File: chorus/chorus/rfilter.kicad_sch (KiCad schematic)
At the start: 12 parts

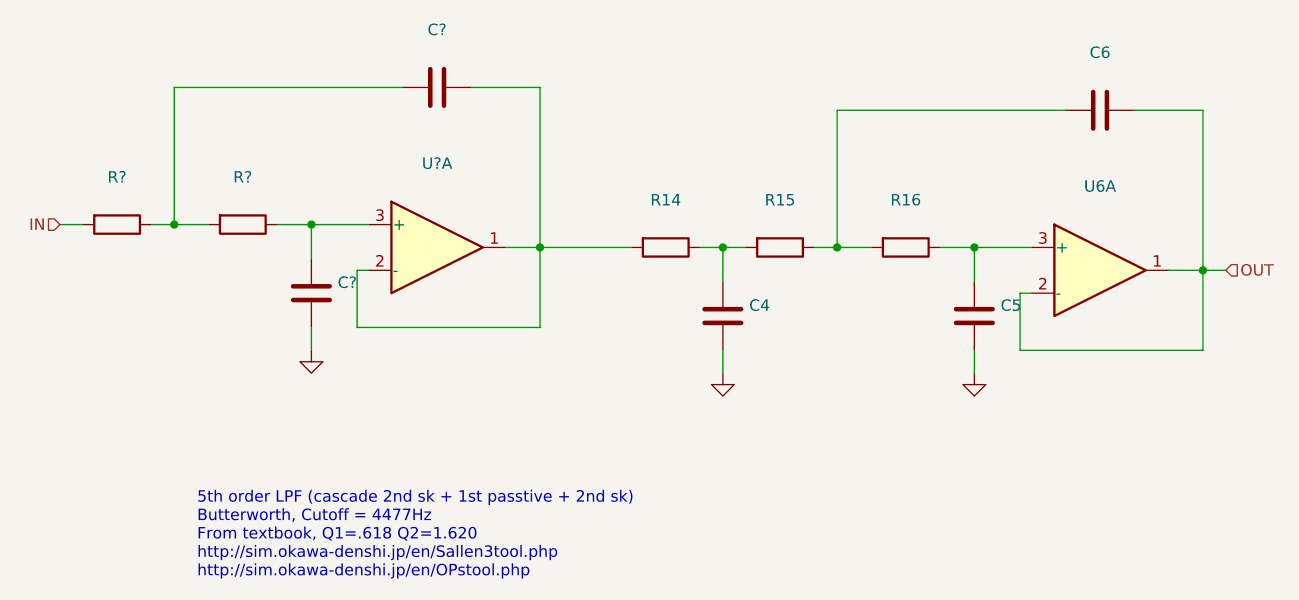
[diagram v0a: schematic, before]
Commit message: add output buffer
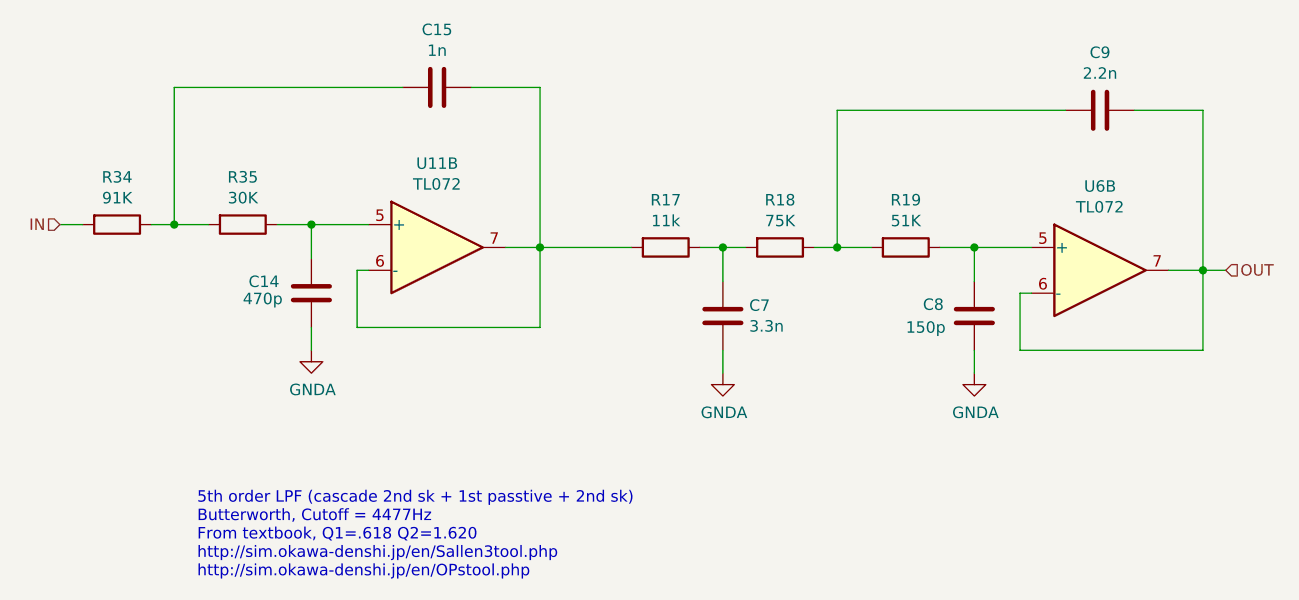
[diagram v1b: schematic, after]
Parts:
- C14: renamed from C?; value (none) -> 470p
- C15: renamed from C?; value (none) -> 1n
- C7: renamed from C4; value (none) -> 3.3n
- C8: renamed from C5; value (none) -> 150p
- C9: renamed from C6; value (none) -> 2.2n
- R17: renamed from R14; value (none) -> 11k
- R18: renamed from R15; value (none) -> 75K
- R19: renamed from R16; value (none) -> 51K
- R34: renamed from R?; value (none) -> 91K
- R35: renamed from R?; value (none) -> 30K
- U11: renamed from U?; value (none) -> TL072
- U6: value (none) -> TL072
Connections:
- net OUT: now also U6.6 (-), U6.7; no longer U6.1, U6.2 (-)
- net at C8.2, R19.1: now also U6.5 (+); no longer U6.3 (+)
- net at C15.1, R17.2: now also U11.6 (-), U11.7; no longer U11.1, U11.2 (-)
- net at C14.2, R35.1: now also U11.5 (+); no longer U11.3 (+)
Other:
- company: (none) -> rabidaudio
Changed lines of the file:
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@@
 (kicad_sch (version 20211123) (generator eeschema)
   (paper "A4")
+  (title_block
+    (company "rabidaudio")
+  )
   (junction (at 109.22 99.06) (diameter 0) (color 0 0 0 0)
   )
@@
     (effects (font (size 1.27 1.27)) (justify right))
   )
-  (symbol (lib_id "Amplifier_Operational:TL072") (at 171.45 101.6 0) (unit 1)
+  (symbol (lib_id "Amplifier_Operational:TL072") (at 171.45 101.6 0) (unit 2)
     (in_bom yes) (on_board yes)
     (property "Reference" "U6" (id 0) (at 171.45 92.2782 0))
-    (property "Value" "" (id 1) (at 171.45 94.5896 0))
+    (property "Value" "TL072" (id 1) (at 171.45 94.5896 0))
     (property "Footprint" "kicad-legacy/Housings_DIP.pretty:DIP-8_W7.62mm" (id 2) (at 171.45 101.6 0)
       (effects (font (size 1.27 1.27)) hide)
@@
   (symbol (lib_id "Device:R") (at 149.86 99.06 270) (unit 1)
     (in_bom yes) (on_board yes)
-    (property "Reference" "R16" (id 0) (at 149.86 93.8022 90))
-    (property "Value" "" (id 1) (at 149.86 96.1136 90))
+    (property "Reference" "R19" (id 0) (at 149.86 93.8022 90))
+    (property "Value" "51K" (id 1) (at 149.86 96.1136 90))
     (property "Footprint" "kicad-legacy/kicad-footprints/Resistor_THT.pretty:R_Axial_DIN0204_L3.6mm_D1.6mm_P2.54mm_Vertical" (id 2) (at 149.86 97.282 90)
       (effects (font (size 1.27 1.27)) hide)
@@
   (symbol (lib_id "Device:R") (at 135.89 99.06 270) (unit 1)
     (in_bom yes) (on_board yes)
-    (property "Reference" "R15" (id 0) (at 135.89 93.8022 90))
-    (property "Value" "" (id 1) (at 135.89 96.1136 90))
+    (property "Reference" "R18" (id 0) (at 135.89 93.8022 90))
+    (property "Value" "75K" (id 1) (at 135.89 96.1136 90))
     (property "Footprint" "kicad-legacy/kicad-footprints/Resistor_THT.pretty:R_Axial_DIN0204_L3.6mm_D1.6mm_P2.54mm_Vertical" (id 2) (at 135.89 97.282 90)
       (effects (font (size 1.27 1.27)) hide)
@@
   (symbol (lib_id "Device:R") (at 123.19 99.06 270) (unit 1)
     (in_bom yes) (on_board yes)
-    (property "Reference" "R14" (id 0) (at 123.19 93.8022 90))
-    (property "Value" "" (id 1) (at 123.19 96.1136 90))
+    (property "Reference" "R17" (id 0) (at 123.19 93.8022 90))
+    (property "Value" "11k" (id 1) (at 123.19 96.1136 90))
     (property "Footprint" "kicad-legacy/kicad-footprints/Resistor_THT.pretty:R_Axial_DIN0204_L3.6mm_D1.6mm_P2.54mm_Vertical" (id 2) (at 123.19 97.282 90)
       (effects (font (size 1.27 1.27)) hide)
@@
   (symbol (lib_id "Device:C") (at 171.45 83.82 270) (unit 1)
     (in_bom yes) (on_board yes)
-    (property "Reference" "C6" (id 0) (at 171.45 77.4192 90))
-    (property "Value" "" (id 1) (at 171.45 79.7306 90))
+    (property "Reference" "C9" (id 0) (at 171.45 77.4192 90))
+    (property "Value" "2.2n" (id 1) (at 171.45 79.7306 90))
     (property "Footprint" "" (id 2) (at 167.64 84.7852 0)
       (effects (font (size 1.27 1.27)) hide)
@@
   (symbol (lib_id "Device:C") (at 157.48 106.68 180) (unit 1)
     (in_bom yes) (on_board yes)
-    (property "Reference" "C5" (id 0) (at 160.401 105.5116 0)
-      (effects (font (size 1.27 1.27)) (justify right))
-    )
-    (property "Value" "" (id 1) (at 160.401 107.823 0)
+    (property "Reference" "C8" (id 0) (at 151.765 105.41 0)
+      (effects (font (size 1.27 1.27)) (justify right))
+    )
+    (property "Value" "150p" (id 1) (at 149.86 107.95 0)
       (effects (font (size 1.27 1.27)) (justify right))
     )
@@
   (symbol (lib_id "Device:C") (at 129.54 106.68 180) (unit 1)
     (in_bom yes) (on_board yes)
-    (property "Reference" "C4" (id 0) (at 132.461 105.5116 0)
-      (effects (font (size 1.27 1.27)) (justify right))
-    )
-    (property "Value" "" (id 1) (at 132.461 107.823 0)
+    (property "Reference" "C7" (id 0) (at 132.461 105.5116 0)
+      (effects (font (size 1.27 1.27)) (justify right))
+    )
+    (property "Value" "3.3n" (id 1) (at 132.461 107.823 0)
       (effects (font (size 1.27 1.27)) (justify right))
     )
@@
     (pin "2")
   )
-  (symbol (lib_id "Amplifier_Operational:TL072") (at 97.79 99.06 0) (unit 1)
-    (in_bom yes) (on_board yes)
-    (property "Reference" "U?" (id 0) (at 97.79 89.7382 0))
-    (property "Value" "" (id 1) (at 97.79 92.0496 0))
+  (symbol (lib_id "Amplifier_Operational:TL072") (at 97.79 99.06 0) (unit 2)
+    (in_bom yes) (on_board yes)
+    (property "Reference" "U11" (id 0) (at 97.79 89.7382 0))
+    (property "Value" "TL072" (id 1) (at 97.79 92.0496 0))
     (property "Footprint" "kicad-legacy/Housings_DIP.pretty:DIP-8_W7.62mm" (id 2) (at 97.79 99.06 0)
       (effects (font (size 1.27 1.27)) hide)
@@
   (symbol (lib_id "Device:R") (at 76.2 96.52 270) (unit 1)
     (in_bom yes) (on_board yes)
-    (property "Reference" "R?" (id 0) (at 76.2 91.2622 90))
-    (property "Value" "" (id 1) (at 76.2 93.5736 90))
+    (property "Reference" "R35" (id 0) (at 76.2 91.2622 90))
+    (property "Value" "30K" (id 1) (at 76.2 93.5736 90))
     (property "Footprint" "kicad-legacy/kicad-footprints/Resistor_THT.pretty:R_Axial_DIN0204_L3.6mm_D1.6mm_P2.54mm_Vertical" (id 2) (at 76.2 94.742 90)
       (effects (font (size 1.27 1.27)) hide)
@@
   (symbol (lib_id "Device:R") (at 62.23 96.52 270) (unit 1)
     (in_bom yes) (on_board yes)
-    (property "Reference" "R?" (id 0) (at 62.23 91.2622 90))
-    (property "Value" "" (id 1) (at 62.23 93.5736 90))
+    (property "Reference" "R34" (id 0) (at 62.23 91.2622 90))
+    (property "Value" "91K" (id 1) (at 62.23 93.5736 90))
     (property "Footprint" "kicad-legacy/kicad-footprints/Resistor_THT.pretty:R_Axial_DIN0204_L3.6mm_D1.6mm_P2.54mm_Vertical" (id 2) (at 62.23 94.742 90)
       (effects (font (size 1.27 1.27)) hide)
@@
   (symbol (lib_id "Device:C") (at 97.79 81.28 270) (unit 1)
     (in_bom yes) (on_board yes)
-    (property "Reference" "C?" (id 0) (at 97.79 74.8792 90))
-    (property "Value" "" (id 1) (at 97.79 77.1906 90))
+    (property "Reference" "C15" (id 0) (at 97.79 74.8792 90))
+    (property "Value" "1n" (id 1) (at 97.79 77.1906 90))
     (property "Footprint" "" (id 2) (at 93.98 82.2452 0)
       (effects (font (size 1.27 1.27)) hide)
@@
   (symbol (lib_id "Device:C") (at 83.82 104.14 180) (unit 1)
     (in_bom yes) (on_board yes)
-    (property "Reference" "C?" (id 0) (at 86.741 102.9716 0)
-      (effects (font (size 1.27 1.27)) (justify right))
-    )
-    (property "Value" "" (id 1) (at 86.741 105.283 0)
+    (property "Reference" "C14" (id 0) (at 76.835 102.87 0)
+      (effects (font (size 1.27 1.27)) (justify right))
+    )
+    (property "Value" "470p" (id 1) (at 76.2 104.775 0)
       (effects (font (size 1.27 1.27)) (justify right))
     )
@@
   (symbol (lib_id "power:GNDA") (at 83.82 110.49 0) (unit 1)
     (in_bom yes) (on_board yes)
-    (property "Reference" "#PWR?" (id 0) (at 83.82 116.84 0)
-      (effects (font (size 1.27 1.27)) hide)
-    )
-    (property "Value" "" (id 1) (at 83.947 114.8842 0))
+    (property "Reference" "#PWR06" (id 0) (at 83.82 116.84 0)
+      (effects (font (size 1.27 1.27)) hide)
+    )
+    (property "Value" "GNDA" (id 1) (at 83.947 114.8842 0))
     (property "Footprint" "" (id 2) (at 83.82 110.49 0)
       (effects (font (size 1.27 1.27)) hide)
@@
   (symbol (lib_id "power:GNDA") (at 129.54 113.03 0) (unit 1)
     (in_bom yes) (on_board yes)
-    (property "Reference" "#PWR?" (id 0) (at 129.54 119.38 0)
-      (effects (font (size 1.27 1.27)) hide)
-    )
-    (property "Value" "" (id 1) (at 129.667 117.4242 0))
+    (property "Reference" "#PWR0110" (id 0) (at 129.54 119.38 0)
+      (effects (font (size 1.27 1.27)) hide)
+    )
+    (property "Value" "GNDA" (id 1) (at 129.667 117.4242 0))
     (property "Footprint" "" (id 2) (at 129.54 113.03 0)
       (effects (font (size 1.27 1.27)) hide)
@@
   (symbol (lib_id "power:GNDA") (at 157.48 113.03 0) (unit 1)
     (in_bom yes) (on_board yes)
-    (property "Reference" "#PWR?" (id 0) (at 157.48 119.38 0)
-      (effects (font (size 1.27 1.27)) hide)
-    )
-    (property "Value" "" (id 1) (at 157.607 117.4242 0))
+    (property "Reference" "#PWR0112" (id 0) (at 157.48 119.38 0)
+      (effects (font (size 1.27 1.27)) hide)
+    )
+    (property "Value" "GNDA" (id 1) (at 157.607 117.4242 0))
     (property "Footprint" "" (id 2) (at 157.48 113.03 0)
       (effects (font (size 1.27 1.27)) hide)
